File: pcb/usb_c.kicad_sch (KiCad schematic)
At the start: 6 parts, among them J8 USB_C_Receptacle_USB2.0_14P, U7 TPS2051CDBV, U8 USBLC6-2SC6

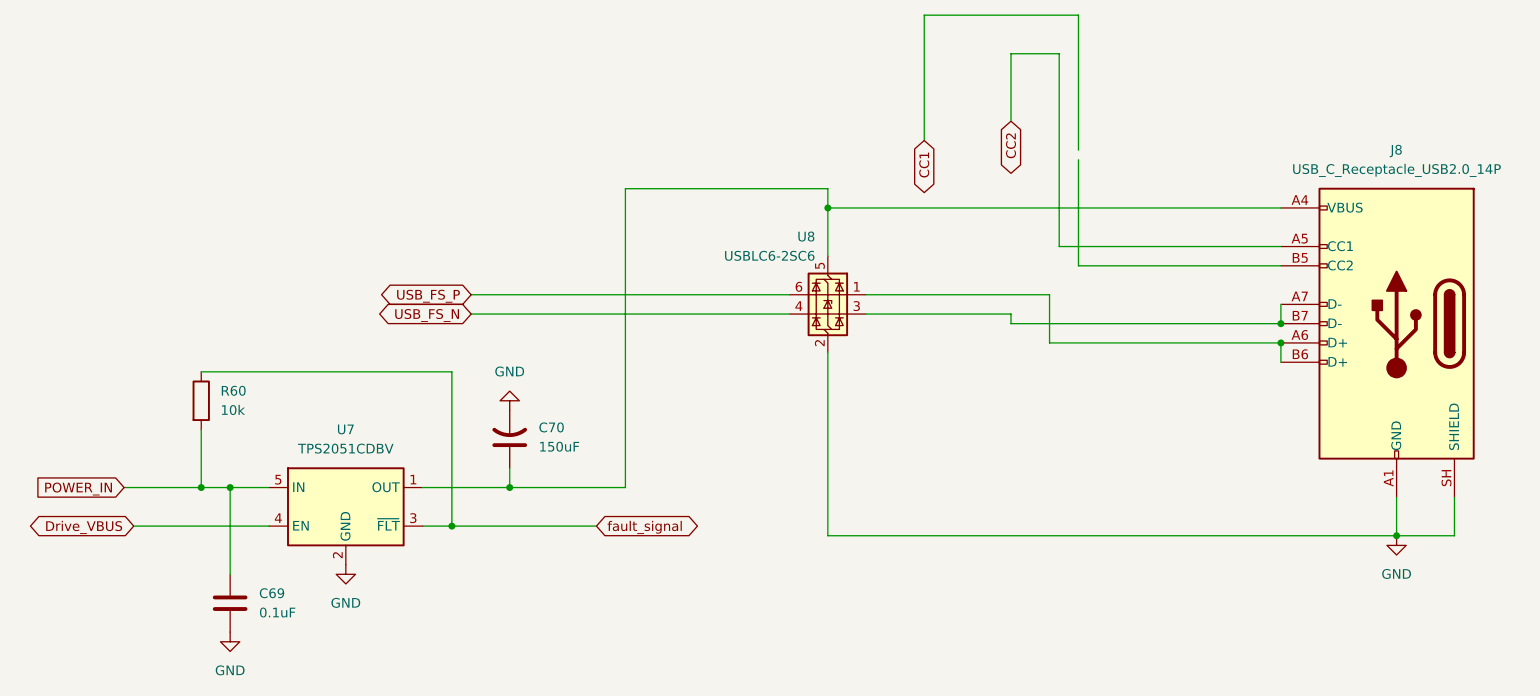
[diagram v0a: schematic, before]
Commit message: pcb: simplify mcu led
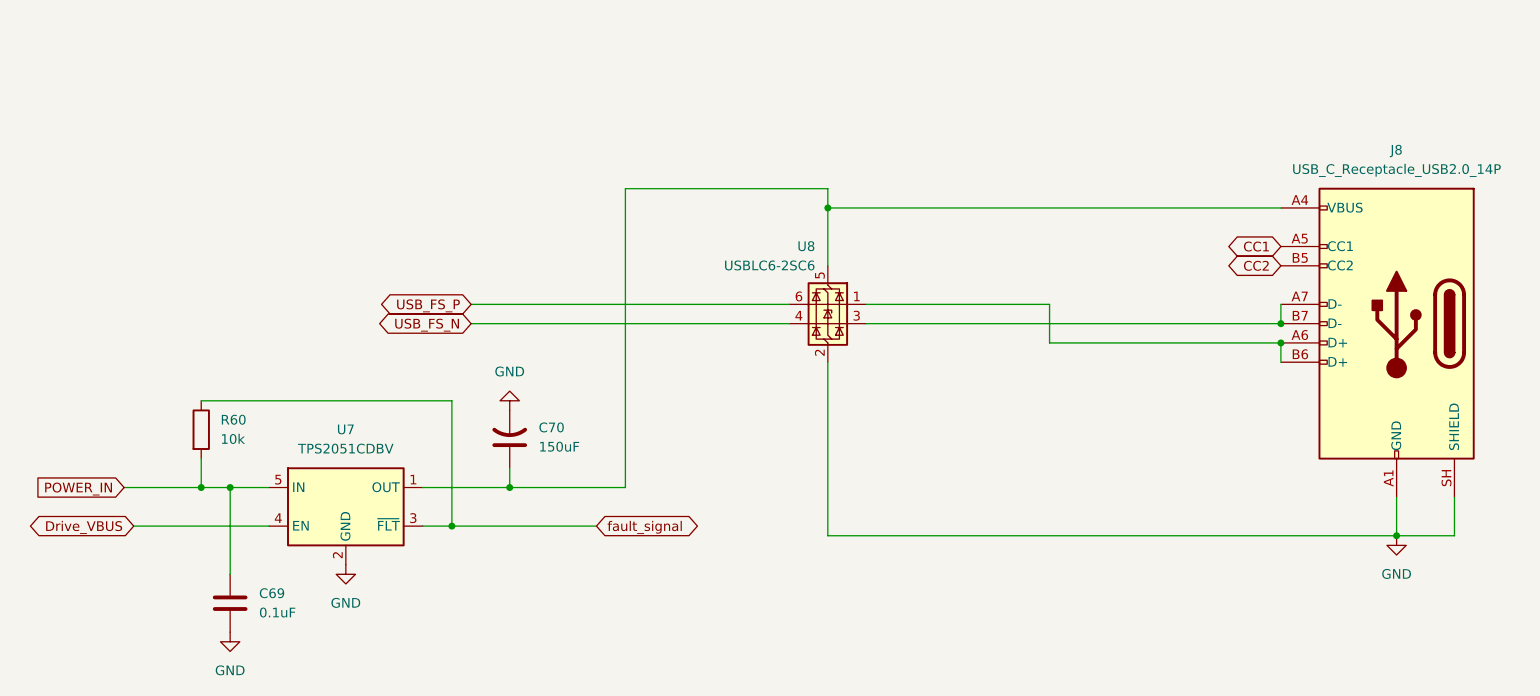
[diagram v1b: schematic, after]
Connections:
- net CC1: now also J8.A5 (CC1)
- net CC2: now also J8.B5 (CC2); no longer J8.A5 (CC1)
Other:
- moved on the sheet: R60, U8
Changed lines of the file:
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@@
+	)
+	(junction
+		(at 41.91 111.76)
+		(diameter 0)
+		(color 0 0 0 0)
 	)
 	(junction
@@
 	)
 	(junction
-		(at 41.91 111.76)
-		(diameter 0)
-		(color 0 0 0 0)
-	)
-	(junction
 		(at 45.72 111.76)
 		(diameter 0)
@@
 	(wire
 		(pts
-			(xy 157.48 82.55) (xy 184.15 82.55)
-		)
-		(stroke
-			(width 0)
-			(type default)
-		)
-	)
-	(wire
-		(pts
-			(xy 157.48 68.58) (xy 157.48 82.55)
-		)
-		(stroke
-			(width 0)
-			(type default)
-		)
-	)
-	(wire
-		(pts
-			(xy 154.94 54.61) (xy 148.59 54.61)
-		)
-		(stroke
-			(width 0)
-			(type default)
-		)
-	)
-	(wire
-		(pts
 			(xy 199.39 113.03) (xy 199.39 118.11)
 		)
@@
 	(wire
 		(pts
-			(xy 157.48 49.53) (xy 137.16 49.53)
-		)
-		(stroke
-			(width 0)
-			(type default)
-		)
-	)
-	(wire
-		(pts
-			(xy 157.48 67.31) (xy 157.48 49.53)
-		)
-		(stroke
-			(width 0)
-			(type default)
-		)
-	)
-	(wire
-		(pts
-			(xy 124.46 74.93) (xy 124.46 81.28)
+			(xy 124.46 74.93) (xy 124.46 82.55)
 		)
 		(stroke
@@
 	(wire
 		(pts
-			(xy 129.54 88.9) (xy 148.59 88.9)
+			(xy 129.54 90.17) (xy 184.15 90.17)
 		)
 		(stroke
@@
 	(wire
 		(pts
-			(xy 77.47 88.9) (xy 119.38 88.9)
-		)
-		(stroke
-			(width 0)
-			(type default)
-		)
-	)
-	(wire
-		(pts
 			(xy 184.15 92.71) (xy 184.15 95.25)
 		)
@@
 	(wire
 		(pts
-			(xy 137.16 49.53) (xy 137.16 66.04)
-		)
-		(stroke
-			(width 0)
-			(type default)
-		)
-	)
-	(wire
-		(pts
 			(xy 45.72 111.76) (xy 45.72 123.19)
 		)
@@
 	(wire
 		(pts
-			(xy 148.59 54.61) (xy 148.59 63.5)
-		)
-		(stroke
-			(width 0)
-			(type default)
-		)
-	)
-	(wire
-		(pts
 			(xy 124.46 74.93) (xy 184.15 74.93)
 		)
@@
 	(wire
 		(pts
-			(xy 74.93 96.52) (xy 74.93 116.84)
+			(xy 74.93 100.33) (xy 74.93 116.84)
 		)
 		(stroke
@@
 	(wire
 		(pts
-			(xy 154.94 80.01) (xy 184.15 80.01)
-		)
-		(stroke
-			(width 0)
-			(type default)
-		)
-	)
-	(wire
-		(pts
-			(xy 41.91 104.14) (xy 41.91 111.76)
+			(xy 41.91 107.95) (xy 41.91 111.76)
 		)
 		(stroke
@@
 	(wire
 		(pts
-			(xy 148.59 90.17) (xy 148.59 88.9)
+			(xy 77.47 87.63) (xy 119.38 87.63)
 		)
 		(stroke
@@
 	(wire
 		(pts
-			(xy 184.15 90.17) (xy 148.59 90.17)
-		)
-		(stroke
-			(width 0)
-			(type default)
-		)
-	)
-	(wire
-		(pts
 			(xy 41.91 111.76) (xy 45.72 111.76)
 		)
@@
 	(wire
 		(pts
-			(xy 124.46 93.98) (xy 124.46 118.11)
+			(xy 77.47 90.17) (xy 119.38 90.17)
+		)
+		(stroke
+			(width 0)
+			(type default)
+		)
+	)
+	(wire
+		(pts
+			(xy 124.46 95.25) (xy 124.46 118.11)
 		)
 		(stroke
@@
 	(wire
 		(pts
-			(xy 41.91 96.52) (xy 74.93 96.52)
-		)
-		(stroke
-			(width 0)
-			(type default)
-		)
-	)
-	(wire
-		(pts
-			(xy 77.47 86.36) (xy 119.38 86.36)
+			(xy 41.91 100.33) (xy 74.93 100.33)
 		)
 		(stroke
@@
 	(wire
 		(pts
-			(xy 154.94 80.01) (xy 154.94 54.61)
-		)
-		(stroke
-			(width 0)
-			(type default)
-		)
-	)
-	(wire
-		(pts
 			(xy 33.02 116.84) (xy 50.8 116.84)
 		)
@@
 	(wire
 		(pts
-			(xy 153.67 86.36) (xy 153.67 92.71)
-		)
-		(stroke
-			(width 0)
-			(type default)
-		)
-	)
-	(wire
-		(pts
-			(xy 153.67 86.36) (xy 129.54 86.36)
+			(xy 153.67 87.63) (xy 153.67 92.71)
+		)
+		(stroke
+			(width 0)
+			(type default)
+		)
+	)
+	(wire
+		(pts
+			(xy 153.67 87.63) (xy 129.54 87.63)
 		)
 		(stroke
@@
 	(global_label "CC2"
 		(shape bidirectional)
-		(at 148.59 63.5 270)
+		(at 184.15 82.55 180)
 		(fields_autoplaced yes)
 		(effects
@@
 		)
 		(property "Intersheetrefs" "${INTERSHEET_REFS}"
-			(at 148.59 71.346 90)
+			(at 176.304 82.55 0)
 			(hide yes)
 			(show_name no)
@@
 	(global_label "USB_FS_P"
 		(shape bidirectional)
-		(at 77.47 86.36 180)
+		(at 77.47 87.63 180)
 		(fields_autoplaced yes)
 		(effects
@@
 		)
 		(property "Intersheetrefs" "${INTERSHEET_REFS}"
-			(at 64.0602 86.36 0)
+			(at 64.0602 87.63 0)
 			(hide yes)
 			(show_name no)
@@
 	(global_label "CC1"
 		(shape bidirectional)
-		(at 137.16 66.04 270)
+		(at 184.15 80.01 180)
 		(fields_autoplaced yes)
 		(effects
@@
 		)
 		(property "Intersheetrefs" "${INTERSHEET_REFS}"
-			(at 137.16 73.886 90)
+			(at 176.304 80.01 0)
 			(hide yes)
 			(show_name no)
@@
 	(global_label "USB_FS_N"
 		(shape bidirectional)
-		(at 77.47 88.9 180)
+		(at 77.47 90.17 180)
 		(fields_autoplaced yes)
 		(effects
@@
 		)
 		(property "Intersheetrefs" "${INTERSHEET_REFS}"
-			(at 63.9997 88.9 0)
+			(at 63.9997 90.17 0)
 			(hide yes)
 			(show_name no)
@@
 	(symbol
 		(lib_id "Device:R")
-		(at 41.91 100.33 0)
+		(at 41.91 104.14 0)
 		(unit 1)
 		(body_style 1)
@@
 		(fields_autoplaced yes)
 		(property "Reference" "R60"
-			(at 44.45 99.0599 0)
+			(at 44.45 102.8699 0)
 			(show_name no)
 			(do_not_autoplace no)
@@
 		)
 		(property "Value" "10k"
-			(at 44.45 101.5999 0)
+			(at 44.45 105.4099 0)
 			(show_name no)
 			(do_not_autoplace no)
@@
 		)
 		(property "Footprint" "Resistor_SMD:R_0805_2012Metric_Pad1.20x1.40mm_HandSolder"
-			(at 40.132 100.33 90)
+			(at 40.132 104.14 90)
 			(hide yes)
 			(show_name no)
@@
 		)
 		(property "Datasheet" ""
-			(at 41.91 100.33 0)
+			(at 41.91 104.14 0)
 			(hide yes)
 			(show_name no)
@@
 		)
 		(property "Description" "Resistor"
-			(at 41.91 100.33 0)
+			(at 41.91 104.14 0)
 			(hide yes)
 			(show_name no)
@@
 	(symbol
 		(lib_id "Power_Protection:USBLC6-2SC6")
-		(at 124.46 86.36 0)
+		(at 124.46 87.63 0)
 		(mirror y)
 		(unit 1)
@@
 		(dnp no)
 		(property "Reference" "U8"
-			(at 122.8089 78.74 0)
+			(at 122.8089 80.01 0)
 			(show_name no)
 			(do_not_autoplace no)
@@
 		)
 		(property "Value" "USBLC6-2SC6"
-			(at 122.8089 81.28 0)
+			(at 122.8089 82.55 0)
 			(show_name no)
 			(do_not_autoplace no)
@@
 		)
 		(property "Footprint" "Package_TO_SOT_SMD:SOT-23-6"
-			(at 123.19 92.71 0)
+			(at 123.19 93.98 0)
 			(hide yes)
 			(show_name no)
@@
 		)
 		(property "Datasheet" "https://www.st.com/resource/en/datasheet/usblc6-2.pdf"
-			(at 123.19 94.615 0)
+			(at 123.19 95.885 0)
 			(hide yes)
 			(show_name no)
@@
 		)
 		(property "Description" "Very low capacitance ESD protection diode, 2 data-line, SOT-23-6"
-			(at 124.46 86.36 0)
-			(hide yes)
-			(show_name no)
+			(at 124.46 87.63 0)
+			(hide yes)
+			(show_name no)

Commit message: pcb/layout: usbs and pds
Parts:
- J8: footprint USB4110_GF_A:USB4110-GF-A_GCT -> Connector_USB:USB_C_Receptacle_GCT_USB4105-xx-A_16P_TopMnt_Horizontal
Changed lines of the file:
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@@
 			)
 		)
-		(property "Footprint" "USB4110_GF_A:USB4110-GF-A_GCT"
+		(property "Footprint" "Connector_USB:USB_C_Receptacle_GCT_USB4105-xx-A_16P_TopMnt_Horizontal"
 			(at 195.58 90.17 0)
 			(hide yes)

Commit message: added new jumper
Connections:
- net POWER_IN renamed 5V_IN
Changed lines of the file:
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@@
+		)
+	)
+	(label "5V_IN"
+		(at 31.75 111.76 0)
+		(effects
+			(font
+				(size 1.27 1.27)
+			)
+			(justify left bottom)
 		)
 	)
@@
 			)
 		)
-	)
-	(global_label "POWER_IN"
-		(shape input)
-		(at 31.75 111.76 180)
-		(effects
-			(font
-				(size 1.27 1.27)
-			)
-			(justify right)
-		)
-		(property "Intersheetrefs" "${INTERSHEET_REFS}"
-			(at 19.391 111.76 0)
-			(hide yes)
-			(show_name no)
-			(do_not_autoplace no)
-			(effects
-				(font
-					(size 1.27 1.27)
-				)
-				(justify right)
-			)
-		)
-		(property "Extra" "5V"
-			(at 25.4 108.458 0)
-			(show_name no)
-			(do_not_autoplace no)
-			(effects
-				(font
-					(size 1.27 1.27)
-					(color 15 0 171 1)
-				)
-				(justify right)
-			)
-		)

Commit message: added new jumper complete
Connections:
- net 5V_IN renamed POWER_IN
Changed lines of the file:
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@@
-		)
-	)
-	(label "5V_IN"
-		(at 31.75 111.76 0)
-		(effects
-			(font
-				(size 1.27 1.27)
-			)
-			(justify left bottom)
 		)
 	)
@@
 				)
 				(justify right)
+			)
+		)
+	)
+	(global_label "POWER_IN"
+		(shape input)
+		(at 31.75 111.76 180)
+		(effects
+			(font
+				(size 1.27 1.27)
+			)
+			(justify right)
+		)
+		(property "Intersheetrefs" "${INTERSHEET_REFS}"
+			(at 19.391 111.76 0)
+			(hide yes)
+			(show_name no)
+			(do_not_autoplace no)
+			(effects
+				(font
+					(size 1.27 1.27)
+				)
+				(justify right)
+			)
+		)
+		(property "Extra" "5V"
+			(at 28.702 114.3 0)
+			(show_name no)
+			(do_not_autoplace no)
+			(effects
+				(font
+					(size 1.27 1.27)
+					(color 15 0 171 1)
+				)
+				(justify right)

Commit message: labeled usb data +/- conn and diff-paired them
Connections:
- net D+: now reaches J8.A6 (D+), J8.B6 (D+), U8.1 (I/O1)
- net D-: now reaches J8.A7 (D-), J8.B7 (D-), U8.3 (I/O2)
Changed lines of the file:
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@@
+		)
+	)
+	(label "D-"
+		(at 180.34 90.17 0)
+		(effects
+			(font
+				(size 1.27 1.27)
+			)
+			(justify left bottom)
+		)
+	)
+	(label "D+"
+		(at 180.34 92.71 0)
+		(effects
+			(font
+				(size 1.27 1.27)
+			)
+			(justify left bottom)
 		)
 	)

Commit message: redid diff pair usb
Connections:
- net D+: now also U8.3 (I/O2); no longer U8.1 (I/O1)
- net D-: now also U8.1 (I/O1); no longer U8.3 (I/O2)
- net USB_FS_N: now also U8.6 (I/O1); no longer U8.4 (I/O2)
- net USB_FS_P: now also U8.4 (I/O2); no longer U8.6 (I/O1)
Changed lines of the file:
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@@
-	(wire
-		(pts
-			(xy 129.54 90.17) (xy 184.15 90.17)
-		)
-		(stroke
-			(width 0)
-			(type default)
-		)
-	)
 	(wire
 		(pts
@@
 	(wire
 		(pts
+			(xy 77.47 90.17) (xy 119.38 90.17)
+		)
+		(stroke
+			(width 0)
+			(type default)
+		)
+	)
+	(wire
+		(pts
 			(xy 184.15 92.71) (xy 184.15 95.25)
 		)
@@
 	(wire
 		(pts
-			(xy 153.67 92.71) (xy 184.15 92.71)
-		)
-		(stroke
-			(width 0)
-			(type default)
-		)
-	)
-	(wire
-		(pts
 			(xy 45.72 111.76) (xy 45.72 123.19)
 		)
@@
 	(wire
 		(pts
+			(xy 153.67 90.17) (xy 184.15 90.17)
+		)
+		(stroke
+			(width 0)
+			(type default)
+		)
+	)
+	(wire
+		(pts
 			(xy 41.91 107.95) (xy 41.91 111.76)
 		)
@@
 	(wire
 		(pts
+			(xy 153.67 87.63) (xy 153.67 90.17)
+		)
+		(stroke
+			(width 0)
+			(type default)
+		)
+	)
+	(wire
+		(pts
+			(xy 151.13 92.71) (xy 151.13 90.17)
+		)
+		(stroke
+			(width 0)
+			(type default)
+		)
+	)
+	(wire
+		(pts
+			(xy 31.75 111.76) (xy 41.91 111.76)
+		)
+		(stroke
+			(width 0)
+			(type default)
+		)
+	)
+	(wire
+		(pts
+			(xy 74.93 116.84) (xy 93.98 116.84)
+		)
+		(stroke
+			(width 0)
+			(type default)
+		)
+	)
+	(wire
+		(pts
+			(xy 207.01 118.11) (xy 199.39 118.11)
+		)
+		(stroke
+			(width 0)
+			(type default)
+		)
+	)
+	(wire
+		(pts
+			(xy 207.01 113.03) (xy 207.01 118.11)
+		)
+		(stroke
+			(width 0)
+			(type default)
+		)
+	)
+	(wire
+		(pts
+			(xy 41.91 111.76) (xy 45.72 111.76)
+		)
+		(stroke
+			(width 0)
+			(type default)
+		)
+	)
+	(wire
+		(pts
+			(xy 124.46 72.39) (xy 124.46 74.93)
+		)
+		(stroke
+			(width 0)
+			(type default)
+		)
+	)
+	(wire
+		(pts
+			(xy 97.79 72.39) (xy 97.79 111.76)
+		)
+		(stroke
+			(width 0)
+			(type default)
+		)
+	)
+	(wire
+		(pts
+			(xy 124.46 95.25) (xy 124.46 118.11)
+		)
+		(stroke
+			(width 0)
+			(type default)
+		)
+	)
+	(wire
+		(pts
+			(xy 97.79 72.39) (xy 124.46 72.39)
+		)
+		(stroke
+			(width 0)
+			(type default)
+		)
+	)
+	(wire
+		(pts
+			(xy 41.91 100.33) (xy 74.93 100.33)
+		)
+		(stroke
+			(width 0)
+			(type default)
+		)
+	)
+	(wire
+		(pts
+			(xy 184.15 87.63) (xy 184.15 90.17)
+		)
+		(stroke
+			(width 0)
+			(type default)
+		)
+	)
+	(wire
+		(pts
 			(xy 77.47 87.63) (xy 119.38 87.63)
 		)
@@
 	(wire
 		(pts
-			(xy 31.75 111.76) (xy 41.91 111.76)
-		)
-		(stroke
-			(width 0)
-			(type default)
-		)
-	)
-	(wire
-		(pts
-			(xy 74.93 116.84) (xy 93.98 116.84)
-		)
-		(stroke
-			(width 0)
-			(type default)
-		)
-	)
-	(wire
-		(pts
-			(xy 207.01 118.11) (xy 199.39 118.11)
-		)
-		(stroke
-			(width 0)
-			(type default)
-		)
-	)
-	(wire
-		(pts
-			(xy 207.01 113.03) (xy 207.01 118.11)
-		)
-		(stroke
-			(width 0)
-			(type default)
-		)
-	)
-	(wire
-		(pts
-			(xy 41.91 111.76) (xy 45.72 111.76)
-		)
-		(stroke
-			(width 0)
-			(type default)
-		)
-	)
-	(wire
-		(pts
-			(xy 124.46 72.39) (xy 124.46 74.93)
-		)
-		(stroke
-			(width 0)
-			(type default)
-		)
-	)
-	(wire
-		(pts
-			(xy 97.79 72.39) (xy 97.79 111.76)
-		)
-		(stroke
-			(width 0)
-			(type default)
-		)
-	)
-	(wire
-		(pts
-			(xy 77.47 90.17) (xy 119.38 90.17)
-		)
-		(stroke
-			(width 0)
-			(type default)
-		)
-	)
-	(wire
-		(pts
-			(xy 124.46 95.25) (xy 124.46 118.11)
-		)
-		(stroke
-			(width 0)
-			(type default)
-		)
-	)
-	(wire
-		(pts
-			(xy 97.79 72.39) (xy 124.46 72.39)
-		)
-		(stroke
-			(width 0)
-			(type default)
-		)
-	)
-	(wire
-		(pts
-			(xy 41.91 100.33) (xy 74.93 100.33)
-		)
-		(stroke
-			(width 0)
-			(type default)
-		)
-	)
-	(wire
-		(pts
-			(xy 184.15 87.63) (xy 184.15 90.17)
-		)
-		(stroke
-			(width 0)
-			(type default)
-		)
-	)
-	(wire
-		(pts
 			(xy 33.02 116.84) (xy 50.8 116.84)
 		)
@@
 	(wire
 		(pts
-			(xy 153.67 87.63) (xy 153.67 92.71)
+			(xy 151.13 90.17) (xy 129.54 90.17)
+		)
+		(stroke
+			(width 0)
+			(type default)
+		)
+	)
+	(wire
+		(pts
+			(xy 151.13 92.71) (xy 184.15 92.71)
 		)
 		(stroke
@@
 	(global_label "USB_FS_P"
 		(shape bidirectional)
-		(at 77.47 87.63 180)
-		(fields_autoplaced yes)
-		(effects
-			(font
-				(size 1.27 1.27)
-			)
-			(justify right)
-		)
-		(property "Intersheetrefs" "${INTERSHEET_REFS}"
-			(at 64.0602 87.63 0)
+		(at 77.47 90.17 180)
+		(fields_autoplaced yes)
+		(effects
+			(font
+				(size 1.27 1.27)
+			)
+			(justify right)
+		)
+		(property "Intersheetrefs" "${INTERSHEET_REFS}"
+			(at 64.0602 90.17 0)
 			(hide yes)
 			(show_name no)
@@
 	(global_label "USB_FS_N"
 		(shape bidirectional)
-		(at 77.47 90.17 180)
-		(fields_autoplaced yes)
-		(effects
-			(font
-				(size 1.27 1.27)
-			)
-			(justify right)
-		)
-		(property "Intersheetrefs" "${INTERSHEET_REFS}"
-			(at 63.9997 90.17 0)
-			(hide yes)
-			(show_name no)
+		(at 77.47 87.63 180)
+		(fields_autoplaced yes)
+		(effects
+			(font
+				(size 1.27 1.27)
+			)
+			(justify right)
+		)
+		(property "Intersheetrefs" "${INTERSHEET_REFS}"
+			(at 63.9997 87.63 0)
+			(hide yes)
+			(show_name no)

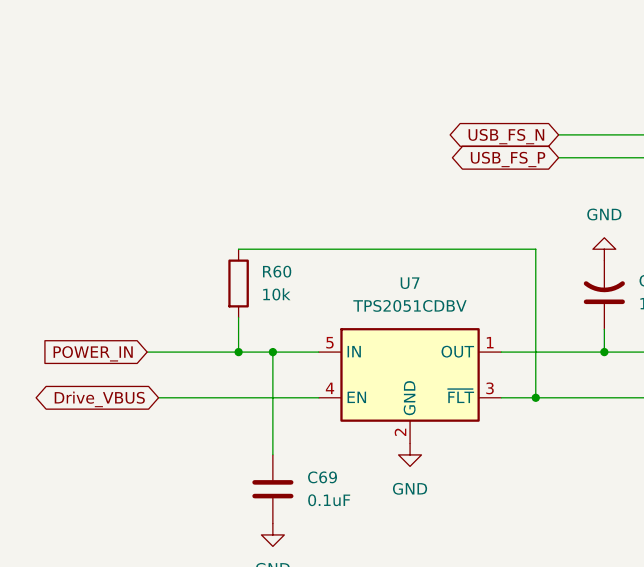
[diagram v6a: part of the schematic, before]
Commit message: made R60 to do not solder
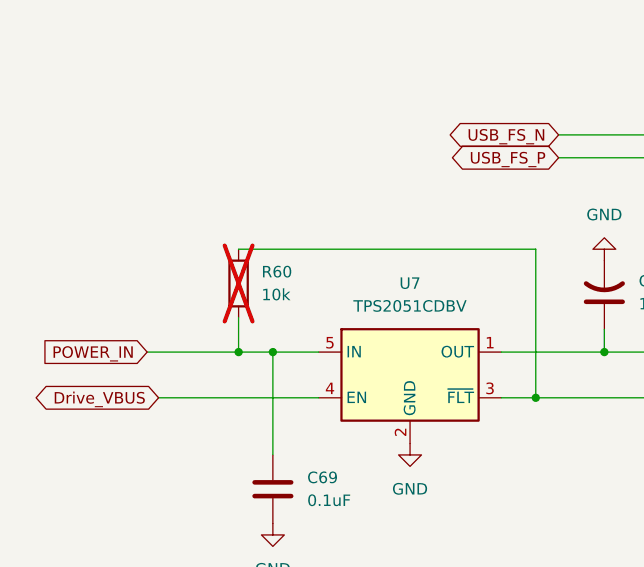
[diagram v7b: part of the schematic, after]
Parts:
- R60: now not fitted
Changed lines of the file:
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@@
 		(on_board yes)
 		(in_pos_files yes)
-		(dnp no)
+		(dnp yes)
 		(fields_autoplaced yes)
 		(property "Reference" "R60"
